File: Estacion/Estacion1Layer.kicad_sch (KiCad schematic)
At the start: 13 parts, among them SW1 SW_Push, U4 WeMos_S2_mini, U5 DHT22, U6 FN-M16P

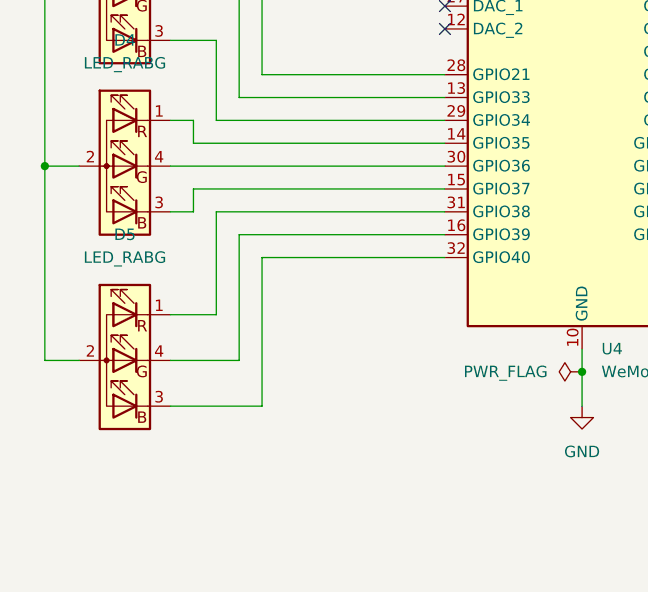
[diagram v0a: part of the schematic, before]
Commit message: Añadir versiones de pcb para dos capas y una capa
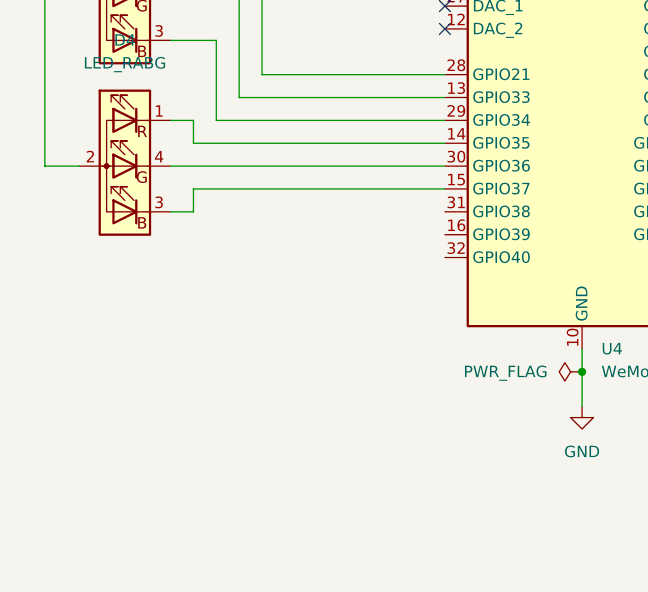
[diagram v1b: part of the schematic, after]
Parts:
- removed D5: LED_RABG, LED_THT:LED_D5.0mm-4_RGB, symbol Device:LED_RABG
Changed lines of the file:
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@@
 		(color 0 0 0 0)
 	)
-	(junction
-		(at 64.77 90.17)
-		(diameter 0)
-		(color 0 0 0 0)
-	)
 	(no_connect
 		(at 139.7 67.31)
@@
 	(wire
 		(pts
-			(xy 88.9 100.33) (xy 109.22 100.33)
-		)
-		(stroke
-			(width 0)
-			(type default)
-		)
-	)
-	(wire
-		(pts
 			(xy 132.08 152.4) (xy 132.08 144.78)
 		)
@@
 	(wire
 		(pts
-			(xy 86.36 111.76) (xy 86.36 97.79)
-		)
-		(stroke
-			(width 0)
-			(type default)
-		)
-	)
-	(wire
-		(pts
 			(xy 139.7 85.09) (xy 143.51 85.09)
 		)
@@
 	(wire
 		(pts
-			(xy 78.74 111.76) (xy 86.36 111.76)
-		)
-		(stroke
-			(width 0)
-			(type default)
-		)
-	)
-	(wire
-		(pts
 			(xy 78.74 71.12) (xy 86.36 71.12)
 		)
@@
 	(wire
 		(pts
-			(xy 83.82 95.25) (xy 109.22 95.25)
-		)
-		(stroke
-			(width 0)
-			(type default)
-		)
-	)
-	(wire
-		(pts
 			(xy 139.7 90.17) (xy 165.1 90.17)
 		)
@@
 	(wire
 		(pts
-			(xy 78.74 106.68) (xy 83.82 106.68)
-		)
-		(stroke
-			(width 0)
-			(type default)
-		)
-	)
-	(wire
-		(pts
 			(xy 165.1 90.17) (xy 165.1 99.06)
 		)
@@
 	(wire
 		(pts
-			(xy 64.77 111.76) (xy 68.58 111.76)
-		)
-		(stroke
-			(width 0)
-			(type default)
-		)
-	)
-	(wire
-		(pts
 			(xy 162.56 92.71) (xy 139.7 92.71)
 		)
@@
 	(wire
 		(pts
-			(xy 86.36 97.79) (xy 109.22 97.79)
-		)
-		(stroke
-			(width 0)
-			(type default)
-		)
-	)
-	(wire
-		(pts
 			(xy 78.74 90.17) (xy 109.22 90.17)
 		)
@@
 	(wire
 		(pts
-			(xy 78.74 116.84) (xy 88.9 116.84)
-		)
-		(stroke
-			(width 0)
-			(type default)
-		)
-	)
-	(wire
-		(pts
 			(xy 86.36 82.55) (xy 109.22 82.55)
 		)
@@
 	(wire
 		(pts
-			(xy 83.82 106.68) (xy 83.82 95.25)
-		)
-		(stroke
-			(width 0)
-			(type default)
-		)
-	)
-	(wire
-		(pts
 			(xy 162.56 80.01) (xy 166.37 80.01)
 		)
@@
 		(pts
 			(xy 115.57 147.32) (xy 139.7 147.32)
-		)
-		(stroke
-			(width 0)
-			(type default)
-		)
-	)
-	(wire
-		(pts
-			(xy 88.9 116.84) (xy 88.9 100.33)
-		)
-		(stroke
-			(width 0)
-			(type default)
-		)
-	)
-	(wire
-		(pts
-			(xy 64.77 90.17) (xy 64.77 111.76)
 		)
 		(stroke
@@
 					(unit 1)
 				)
-			)
-		)
-	)
-	(symbol
-		(lib_id "Device:LED_RABG")
-		(at 73.66 111.76 0)
-		(mirror y)
-		(unit 1)
-		(body_style 1)
-		(exclude_from_sim no)
-		(in_bom yes)
-		(on_board yes)
-		(in_pos_files yes)
-		(dnp no)
-		(property "Reference" "D5"
-			(at 73.66 97.79 0)
-			(show_name no)
-			(do_not_autoplace no)
-			(effects
-				(font
-					(size 1.27 1.27)
-				)
-			)
-		)
-		(property "Value" "LED_RABG"
-			(at 73.66 100.33 0)
-			(show_name no)
-			(do_not_autoplace no)
-			(effects
-				(font
-					(size 1.27 1.27)
-				)
-			)
-		)
-		(property "Footprint" "LED_THT:LED_D5.0mm-4_RGB"
-			(at 73.66 113.03 0)
-			(hide yes)
-			(show_name no)
-			(do_not_autoplace no)
-			(effects
-				(font
-					(size 1.27 1.27)
-				)
-			)
-		)
-		(property "Datasheet" ""
-			(at 73.66 113.03 0)
-			(hide yes)
-			(show_name no)
-			(do_not_autoplace no)
-			(effects
-				(font
-					(size 1.27 1.27)
-				)
-			)
-		)
-		(property "Description" "RGB LED, red/anode/blue/green"
-			(at 73.66 111.76 0)
-			(hide yes)
-			(show_name no)
-			(do_not_autoplace no)
-			(effects
-				(font
-					(size 1.27 1.27)
-				)
-			)
-		)
-		(pin "4"
-		)
-		(pin "3"
-		)
-		(pin "2"
-		)
-		(pin "1"
-		)
-		(instances
-			(project "Estacion"
-				(path "/65db9eb0-748a-4b13-b93f-b47348ad70f0"
-					(reference "D5")
-					(unit 1)
-				)
